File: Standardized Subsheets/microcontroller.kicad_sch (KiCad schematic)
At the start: 57 parts, among them J3 Conn_01x02, J4 Conn_01x02, J5 SWD, SW1 SW_SPDT, U2 STM32F105RCTx, U3 SN65HVD230, U4 SN65HVD230, Y1 16MHz

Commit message: numbers
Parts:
- renumbered C3 to C1, C12 to C10, C13 to C11, C14 to C12, C15 to C13, C16 to C14, C4 to C2, C5 to C3, C6 to C4, C7 to C5, C8 to C6, C9 to C7, C10 to C8, C11 to C9, U2 to U1, U3 to U2, U4 to U3

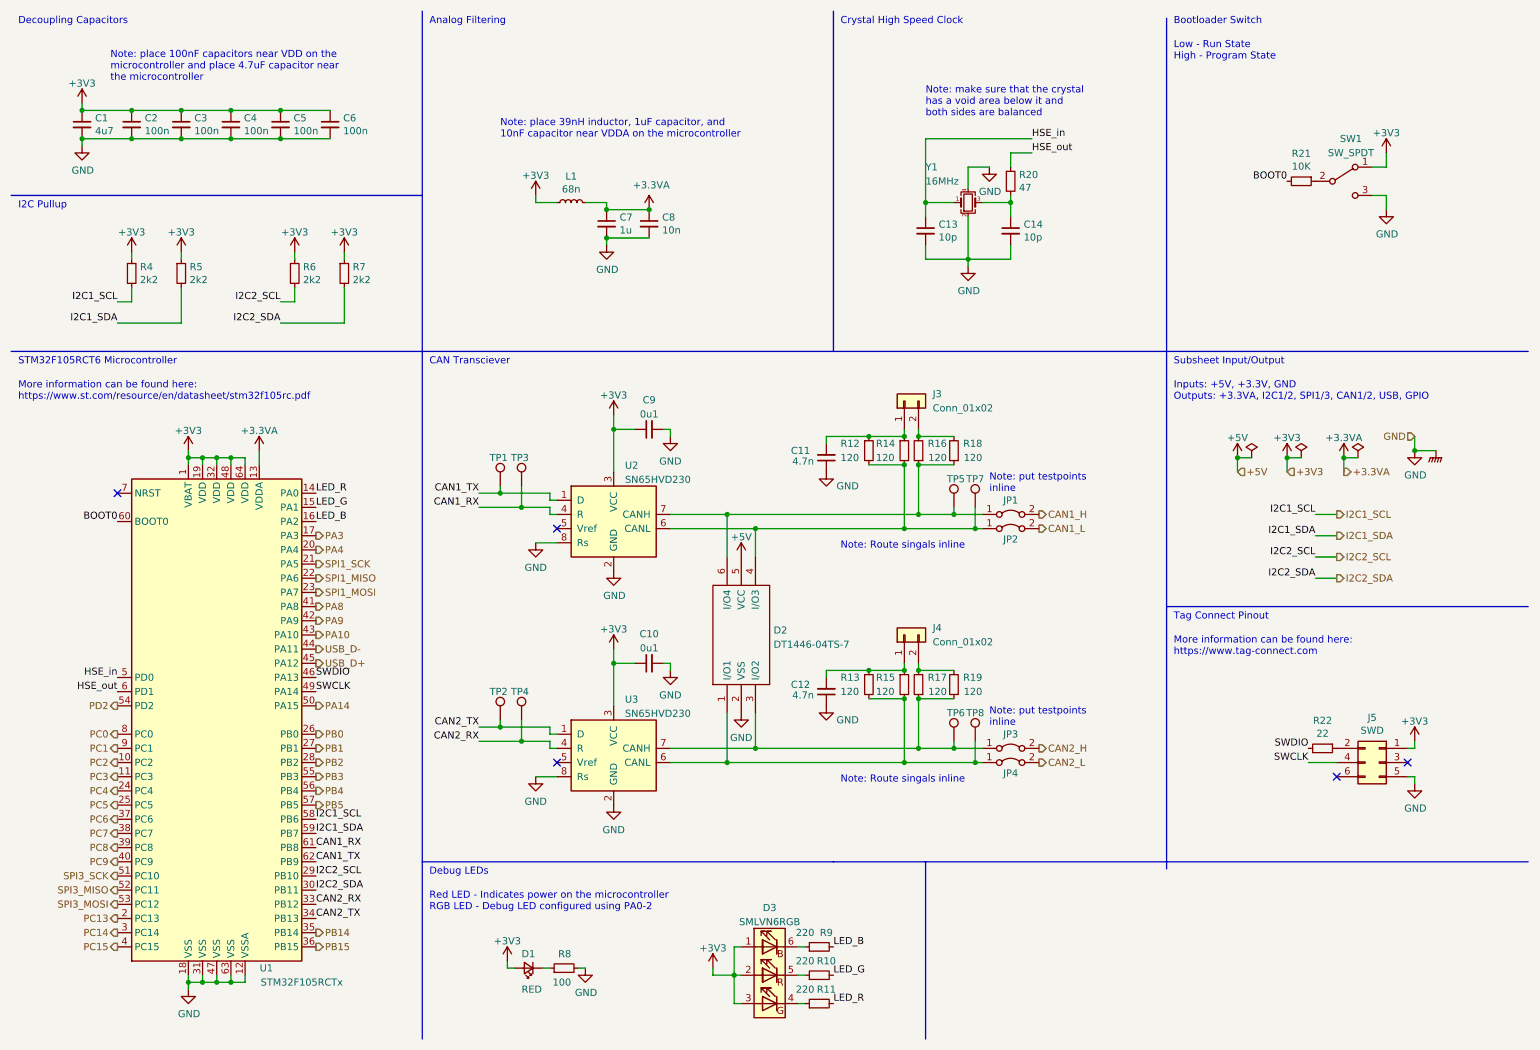
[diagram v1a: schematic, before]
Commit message: adding watchdog
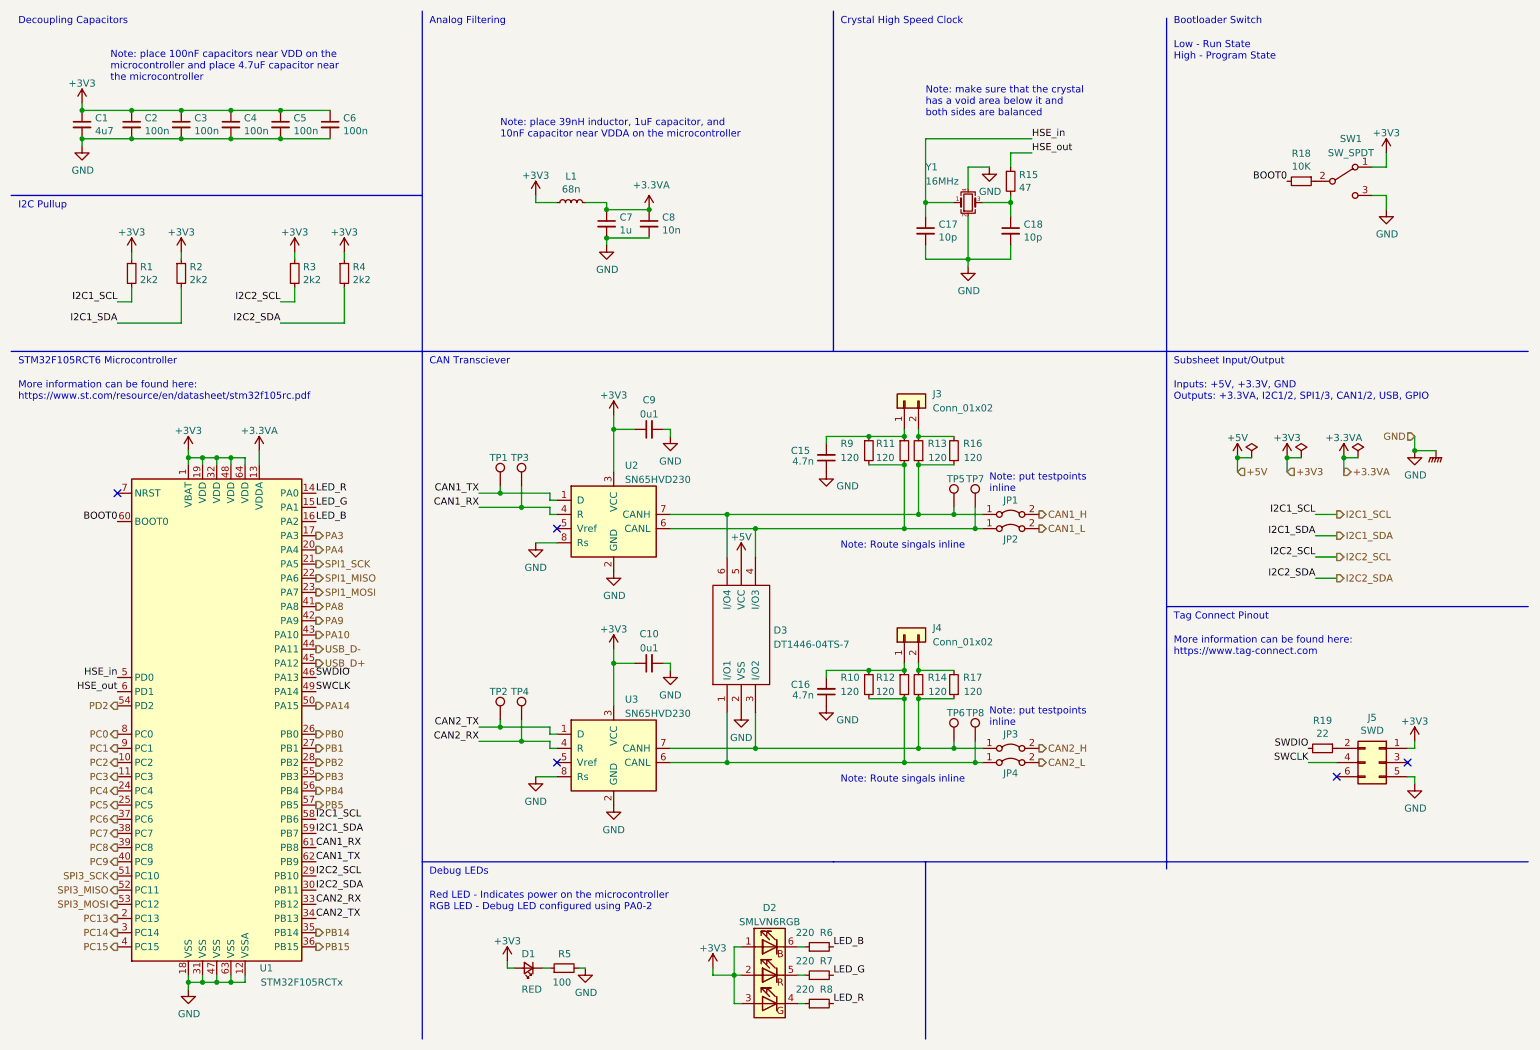
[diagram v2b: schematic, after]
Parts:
- D3: renamed from D2; footprint SOT95P280X100-6N -> Global Libraries:SOT95P280X100-6N
- renumbered C11 to C15, C12 to C16, C13 to C17, C14 to C18, D3 to D2, R4 to R1, R13 to R10, R14 to R11, R15 to R12, R16 to R13, R17 to R14, R20 to R15, R18 to R16, R19 to R17, R21 to R18, R22 to R19, R5 to R2, R6 to R3, R7 to R4, R8 to R5, R9 to R6, R10 to R7, R11 to R8, R12 to R9
